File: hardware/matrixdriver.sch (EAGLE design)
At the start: 46 parts, among them IC1 75176AD, IC2 4017D, IC3 ULN2803, IC4 7805T, J1 DCJ0202, Q1 CSM-7X-DU, Q2 MMBT4403LT1SMD, Q3 MMBT4403LT1SMD, Q4 MMBT4403LT1SMD, Q5 MMBT4403LT1SMD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

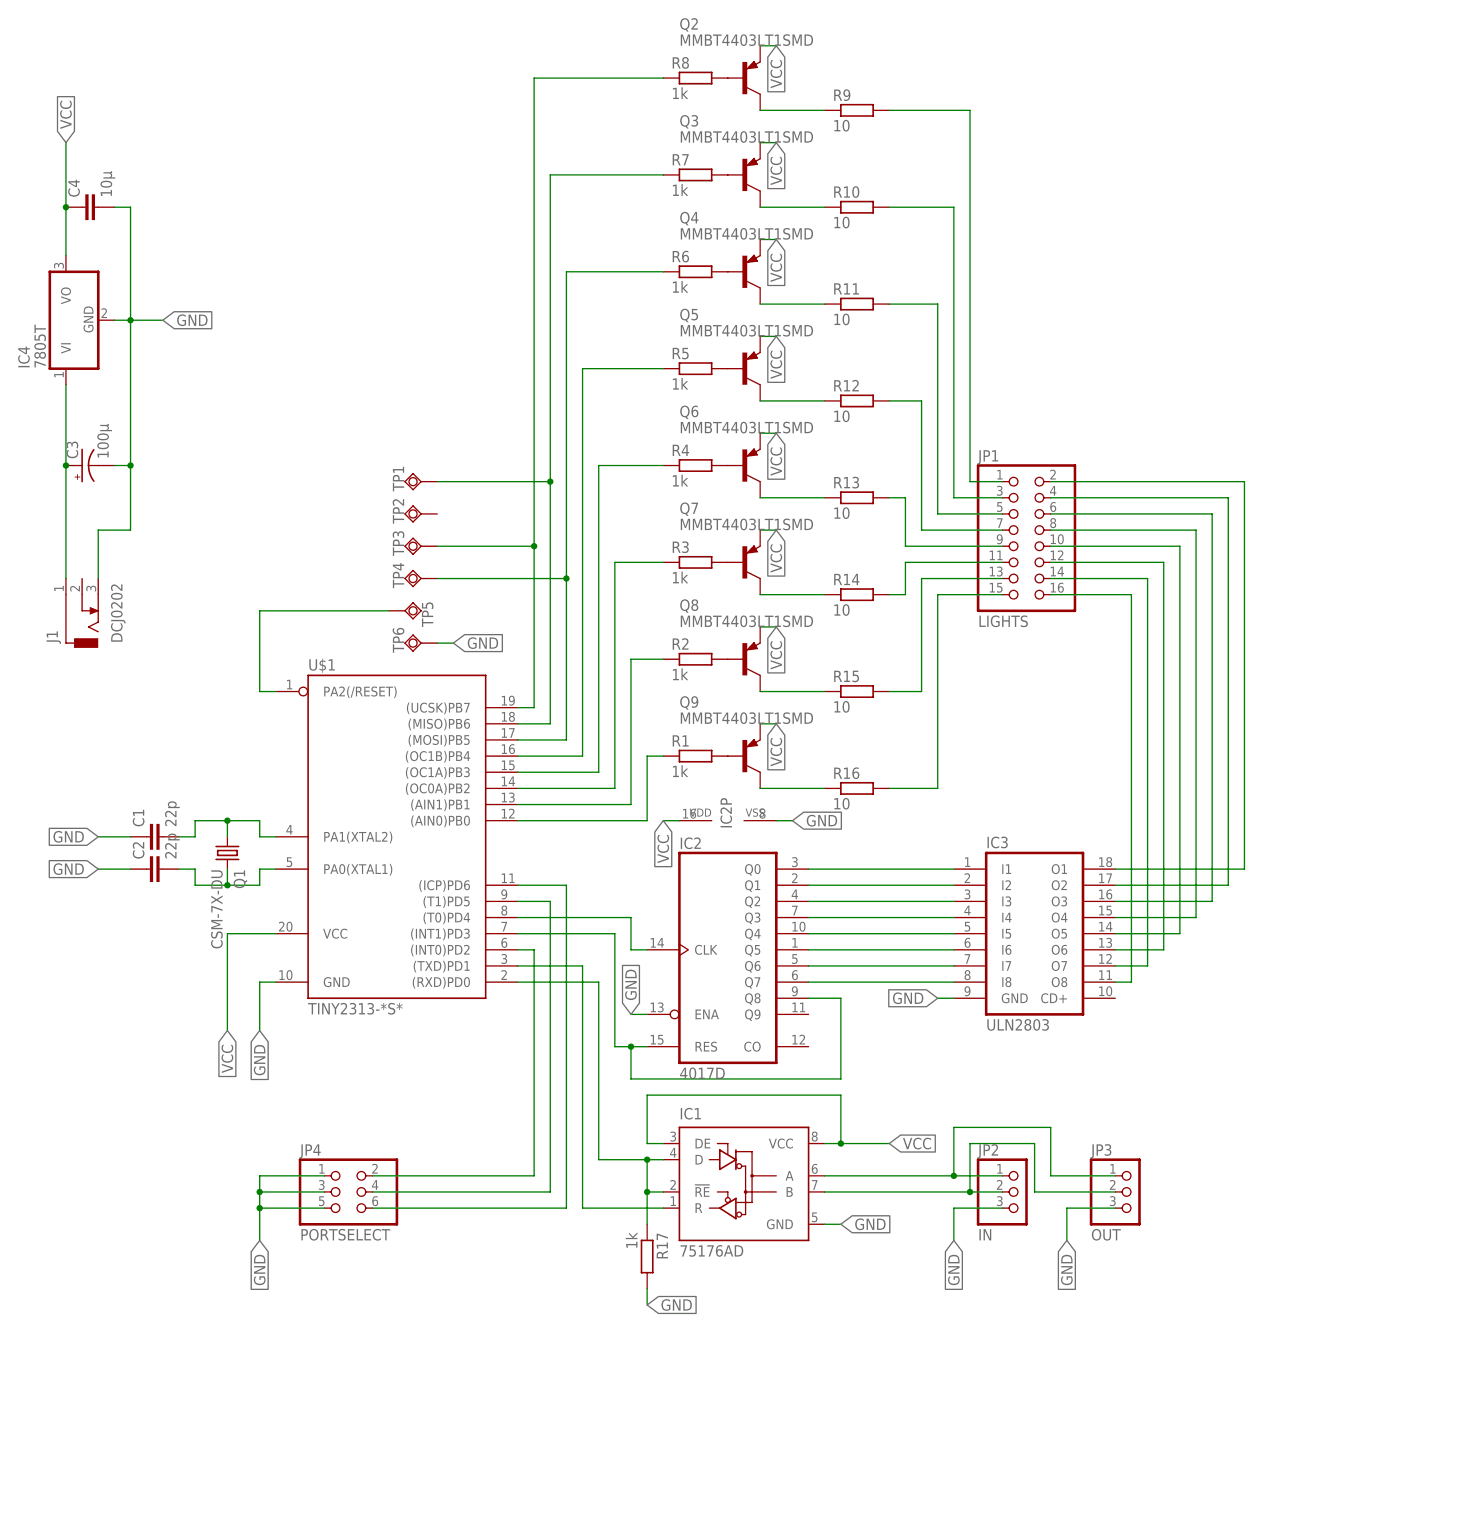
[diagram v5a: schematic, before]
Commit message: Fully routed board
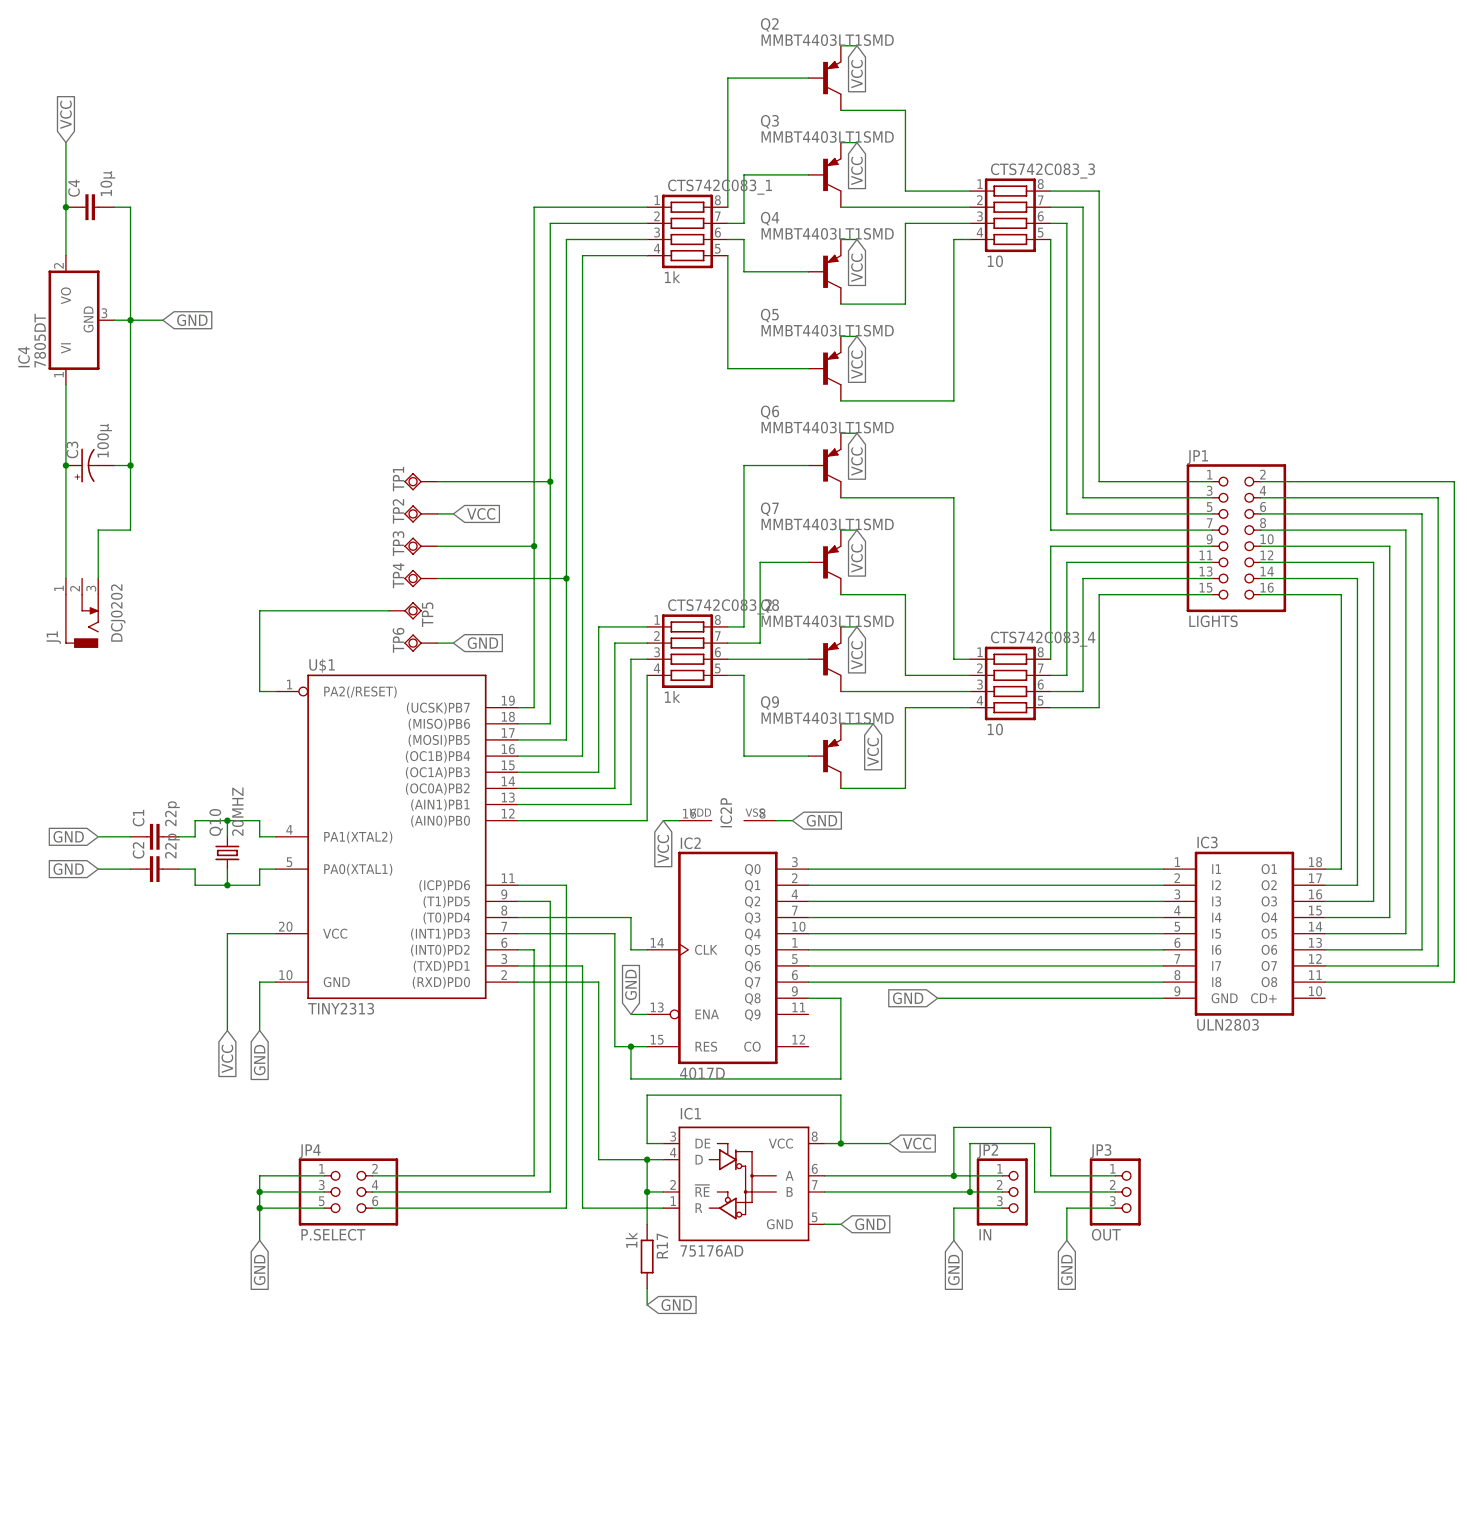
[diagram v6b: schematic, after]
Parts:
- removed Q1: CSM-7X-DU, crystal:CSM-7X-DU
- removed R1, R2, R3, R4, R5, R6, R7, R8: 1k, resistor:R-EU_R1206
- removed R10, R11, R12, R13, R14, R15, R16, R9: 10, resistor:R-EU_R1206
- added CTS742C083_1, CTS742C083_2: 1k, resistor-net:CTS742C083
- added CTS742C083_3, CTS742C083_4: 10, resistor-net:CTS742C083
- added Q10: 20MHZ, adafruit:CRYSTALHC49S
- C3: device rcl:CPOL-USE5-8.5 -> rcl:CPOL-USUD-6,3X5,8
- IC4: value 7805T -> 7805DT; device linear:7805T -> linear:7805DT
- JP1: device pinhead-fixdrills:PINHD-2X8_2.54-90° -> pinhead-fixdrills:PINHD-2X8_2.54
- JP4: value PORTSELECT -> P.SELECT
- TP2: value TPSQTP20SQ -> TPSQTP19SQ; device testpad:TPSQTP20SQ -> testpad:TPSQTP19SQ
- U$1: value TINY2313-*S* -> TINY2313
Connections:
- removed net N$44: Q6.B, R4.2
- removed net N$45: Q5.B, R5.2
- removed net N$46: Q4.B, R6.2
- removed net N$47: Q3.B, R7.2
- removed net N$48: Q2.B, R8.2
- new net N$13: CTS742C083_4.8, JP1.9
- new net N$29: CTS742C083_4.7, JP1.11
- new net N$30: CTS742C083_4.6, JP1.13
- new net N$31: CTS742C083_4.5, JP1.15
- new net N$32: CTS742C083_1.7, Q3.B
- net N$1: now also CTS742C083_2.4; no longer R1.1
- net N$11: now also Q10.2; no longer Q1.1
- net N$12: now also Q10.1; no longer Q1.2
- net N$14: now also IC3.O8; no longer IC3.O1
- net N$2: now also CTS742C083_2.3; no longer R2.1
- net N$25: now also IC3.O1; no longer IC3.O8
- net N$26: now also IC3.O2; no longer IC3.O7
- net N$27: now also IC3.O3; no longer IC3.O6
- net N$28: now also IC3.O4; no longer IC3.O5
- net N$3: now also CTS742C083_2.2; no longer R3.1
- net N$33: now also CTS742C083_3.8; no longer R9.2
- net N$34: now also CTS742C083_3.7; no longer R10.2
- net N$35: now also CTS742C083_3.6; no longer R11.2
- net N$36: now also CTS742C083_3.5; no longer R12.2
- net N$37: now also CTS742C083_1.8, Q2.B; no longer JP1.9, R13.2
- net N$38: now also CTS742C083_1.6, Q4.B; no longer JP1.11, R14.2
- net N$39: now also CTS742C083_1.5, Q5.B; no longer JP1.13, R15.2
- net N$4: now also CTS742C083_2.1; no longer R4.1
- net N$40: now also CTS742C083_2.6, Q8.B; no longer JP1.15, R16.2
- net N$41: now also CTS742C083_2.5; no longer R1.2
- net N$42: now also CTS742C083_2.8, Q6.B; no longer Q8.B, R2.2
- net N$43: now also CTS742C083_2.7; no longer R3.2
- net N$49: now also CTS742C083_4.4; no longer R16.1
- net N$5: now also CTS742C083_1.4; no longer R5.1
- net N$50: now also CTS742C083_4.3; no longer R15.1
- net N$51: now also CTS742C083_4.2; no longer R14.1
- net N$52: now also CTS742C083_4.1; no longer R13.1
- net N$53: now also CTS742C083_3.4; no longer R12.1
- net N$54: now also CTS742C083_3.3; no longer R11.1
- net N$55: now also CTS742C083_3.2; no longer R10.1
- net N$56: now also CTS742C083_3.1; no longer R9.1
- net N$6: now also CTS742C083_1.3; no longer R6.1
- net N$63: now also IC3.O7; no longer IC3.O2
- net N$64: now also IC3.O6; no longer IC3.O3
- net N$66: now also IC3.O5; no longer IC3.O4
- net N$7: now also CTS742C083_1.2; no longer R7.1
- net N$8: now also CTS742C083_1.1; no longer R8.1
- net VCC: now also TP2.TP
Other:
- moved on the sheet: IC3, JP1, Q2, Q3, Q4, Q5, Q6, Q7, Q8, Q9

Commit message: working on a finalised board
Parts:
- added C5: 100n, resistor:C-EUC1206
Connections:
- net GND: now also C5.1
- net VCC: now also C5.2
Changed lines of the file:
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@@
 <?xml version="1.0" encoding="utf-8"?>
 <!DOCTYPE eagle SYSTEM "eagle.dtd">
-<eagle version="6.5.0">
+<eagle version="7.0.0">
 <drawing>
 <settings>
@@
 <grid distance="0.1" unitdist="inch" unit="inch" style="lines" multiple="1" display="no" altdistance="0.01" altunitdist="inch" altunit="inch"/>
 <layers>
-<layer number="1" name="Top" color="4" fill="1" visible="yes" active="no"/>
-<layer number="16" name="Bottom" color="1" fill="1" visible="yes" active="no"/>
-<layer number="17" name="Pads" color="2" fill="1" visible="yes" active="no"/>
-<layer number="18" name="Vias" color="2" fill="1" visible="yes" active="no"/>
-<layer number="19" name="Unrouted" color="6" fill="1" visible="yes" active="no"/>
-<layer number="20" name="Dimension" color="15" fill="1" visible="yes" active="no"/>
-<layer number="21" name="tPlace" color="7" fill="1" visible="yes" active="no"/>
-<layer number="22" name="bPlace" color="7" fill="1" visible="yes" active="no"/>
-<layer number="23" name="tOrigins" color="15" fill="1" visible="yes" active="no"/>
-<layer number="24" name="bOrigins" color="15" fill="1" visible="yes" active="no"/>
-<layer number="25" name="tNames" color="7" fill="1" visible="yes" active="no"/>
-<layer number="26" name="bNames" color="7" fill="1" visible="yes" active="no"/>
-<layer number="27" name="tValues" color="7" fill="1" visible="yes" active="no"/>
-<layer number="28" name="bValues" color="7" fill="1" visible="yes" active="no"/>
+<layer number="1" name="Top" color="4" fill="1" visible="no" active="no"/>
+<layer number="16" name="Bottom" color="1" fill="1" visible="no" active="no"/>
+<layer number="17" name="Pads" color="2" fill="1" visible="no" active="no"/>
+<layer number="18" name="Vias" color="2" fill="1" visible="no" active="no"/>
+<layer number="19" name="Unrouted" color="6" fill="1" visible="no" active="no"/>
+<layer number="20" name="Dimension" color="15" fill="1" visible="no" active="no"/>
+<layer number="21" name="tPlace" color="7" fill="1" visible="no" active="no"/>
+<layer number="22" name="bPlace" color="7" fill="1" visible="no" active="no"/>
+<layer number="23" name="tOrigins" color="15" fill="1" visible="no" active="no"/>
+<layer number="24" name="bOrigins" color="15" fill="1" visible="no" active="no"/>
+<layer number="25" name="tNames" color="7" fill="1" visible="no" active="no"/>
+<layer number="26" name="bNames" color="7" fill="1" visible="no" active="no"/>
+<layer number="27" name="tValues" color="7" fill="1" visible="no" active="no"/>
+<layer number="28" name="bValues" color="7" fill="1" visible="no" active="no"/>
 <layer number="29" name="tStop" color="7" fill="3" visible="no" active="no"/>
 <layer number="30" name="bStop" color="7" fill="6" visible="no" active="no"/>
@@
 <layer number="35" name="tGlue" color="7" fill="4" visible="no" active="no"/>
 <layer number="36" name="bGlue" color="7" fill="5" visible="no" active="no"/>
-<layer number="37" name="tTest" color="7" fill="1" visible="yes" active="no"/>
-<layer number="38" name="bTest" color="7" fill="1" visible="yes" active="no"/>
+<layer number="37" name="tTest" color="7" fill="1" visible="no" active="no"/>
+<layer number="38" name="bTest" color="7" fill="1" visible="no" active="no"/>
 <layer number="39" name="tKeepout" color="4" fill="11" visible="no" active="no"/>
 <layer number="40" name="bKeepout" color="1" fill="11" visible="no" active="no"/>
@@
 <layer number="44" name="Drills" color="7" fill="1" visible="no" active="no"/>
 <layer number="45" name="Holes" color="7" fill="1" visible="no" active="no"/>
-<layer number="46" name="Milling" color="3" fill="1" visible="yes" active="no"/>
-<layer number="47" name="Measures" color="7" fill="1" visible="yes" active="no"/>
-<layer number="48" name="Document" color="7" fill="1" visible="yes" active="no"/>
-<layer number="49" name="Reference" color="7" fill="1" visible="yes" active="no"/>
-<layer number="50" name="dxf" color="7" fill="1" visible="yes" active="no"/>
-<layer number="51" name="tDocu" color="7" fill="1" visible="yes" active="no"/>
-<layer number="52" name="bDocu" color="7" fill="1" visible="yes" active="no"/>
-<layer number="53" name="tGND_GNDA" color="7" fill="9" visible="yes" active="no"/>
-<layer number="54" name="bGND_GNDA" color="1" fill="9" visible="yes" active="no"/>
-<layer number="56" name="wert" color="7" fill="1" visible="yes" active="no"/>
-<layer number="57" name="tCAD" color="7" fill="1" visible="yes" active="no"/>
+<layer number="46" name="Milling" color="3" fill="1" visible="no" active="no"/>
+<layer number="47" name="Measures" color="7" fill="1" visible="no" active="no"/>
+<layer number="48" name="Document" color="7" fill="1" visible="no" active="no"/>
+<layer number="49" name="Reference" color="7" fill="1" visible="no" active="no"/>
+<layer number="50" name="dxf" color="7" fill="1" visible="no" active="no"/>
+<layer number="51" name="tDocu" color="7" fill="1" visible="no" active="no"/>
+<layer number="52" name="bDocu" color="7" fill="1" visible="no" active="no"/>
+<layer number="53" name="tGND_GNDA" color="7" fill="9" visible="no" active="no"/>
+<layer number="54" name="bGND_GNDA" color="1" fill="9" visible="no" active="no"/>
+<layer number="56" name="wert" color="7" fill="1" visible="no" active="no"/>
+<layer number="57" name="tCAD" color="7" fill="1" visible="no" active="no"/>
 <layer number="90" name="Modules" color="5" fill="1" visible="yes" active="yes"/>
 <layer number="91" name="Nets" color="2" fill="1" visible="yes" active="yes"/>
@@
 <part name="CTS742C083_1" library="resistor-net" deviceset="CTS742C083" device="" value="1k"/>
 <part name="CTS742C083_2" library="resistor-net" deviceset="CTS742C083" device="" value="1k"/>
+<part name="C5" library="resistor" deviceset="C-EU" device="C1206" value="100n"/>
 </parts>
 <sheets>
@@
 <instance part="CTS742C083_1" gate="G$1" x="101.6" y="167.64"/>
 <instance part="CTS742C083_2" gate="G$1" x="101.6" y="101.6"/>
+<instance part="C5" gate="G$1" x="35.56" y="50.8" rot="R180"/>
 </instances>
 <busses>
@@
 <segment>
 <pinref part="U$1" gate="G$1" pin="VCC"/>
-<wire x1="38.1" y1="55.88" x2="30.48" y2="55.88" width="0.1524" layer="91"/>
-<wire x1="30.48" y1="55.88" x2="30.48" y2="40.64" width="0.1524" layer="91"/>
-<label x="30.48" y="40.64" size="1.778" layer="95" rot="R270" xref="yes"/>
+<wire x1="38.1" y1="55.88" x2="35.56" y2="55.88" width="0.1524" layer="91"/>
+<wire x1="35.56" y1="55.88" x2="25.4" y2="55.88" width="0.1524" layer="91"/>
+<wire x1="25.4" y1="55.88" x2="25.4" y2="40.64" width="0.1524" layer="91"/>
+<label x="25.4" y="40.64" size="1.778" layer="95" rot="R270" xref="yes"/>
+<pinref part="C5" gate="G$1" pin="2"/>
+<junction x="35.56" y="55.88"/>
 </segment>
 <segment>
@@
 <wire x1="35.56" y1="48.26" x2="35.56" y2="40.64" width="0.1524" layer="91"/>
 <label x="35.56" y="40.64" size="1.778" layer="95" rot="R270" xref="yes"/>
-</segment>
-<segment>
+<pinref part="C5" gate="G$1" pin="1"/>
+<junction x="35.56" y="48.26"/>
+</segment>
+<segment>
